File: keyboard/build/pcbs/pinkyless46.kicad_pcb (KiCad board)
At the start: 2 copper layers, 108.1 x 162.6 mm, 49 parts

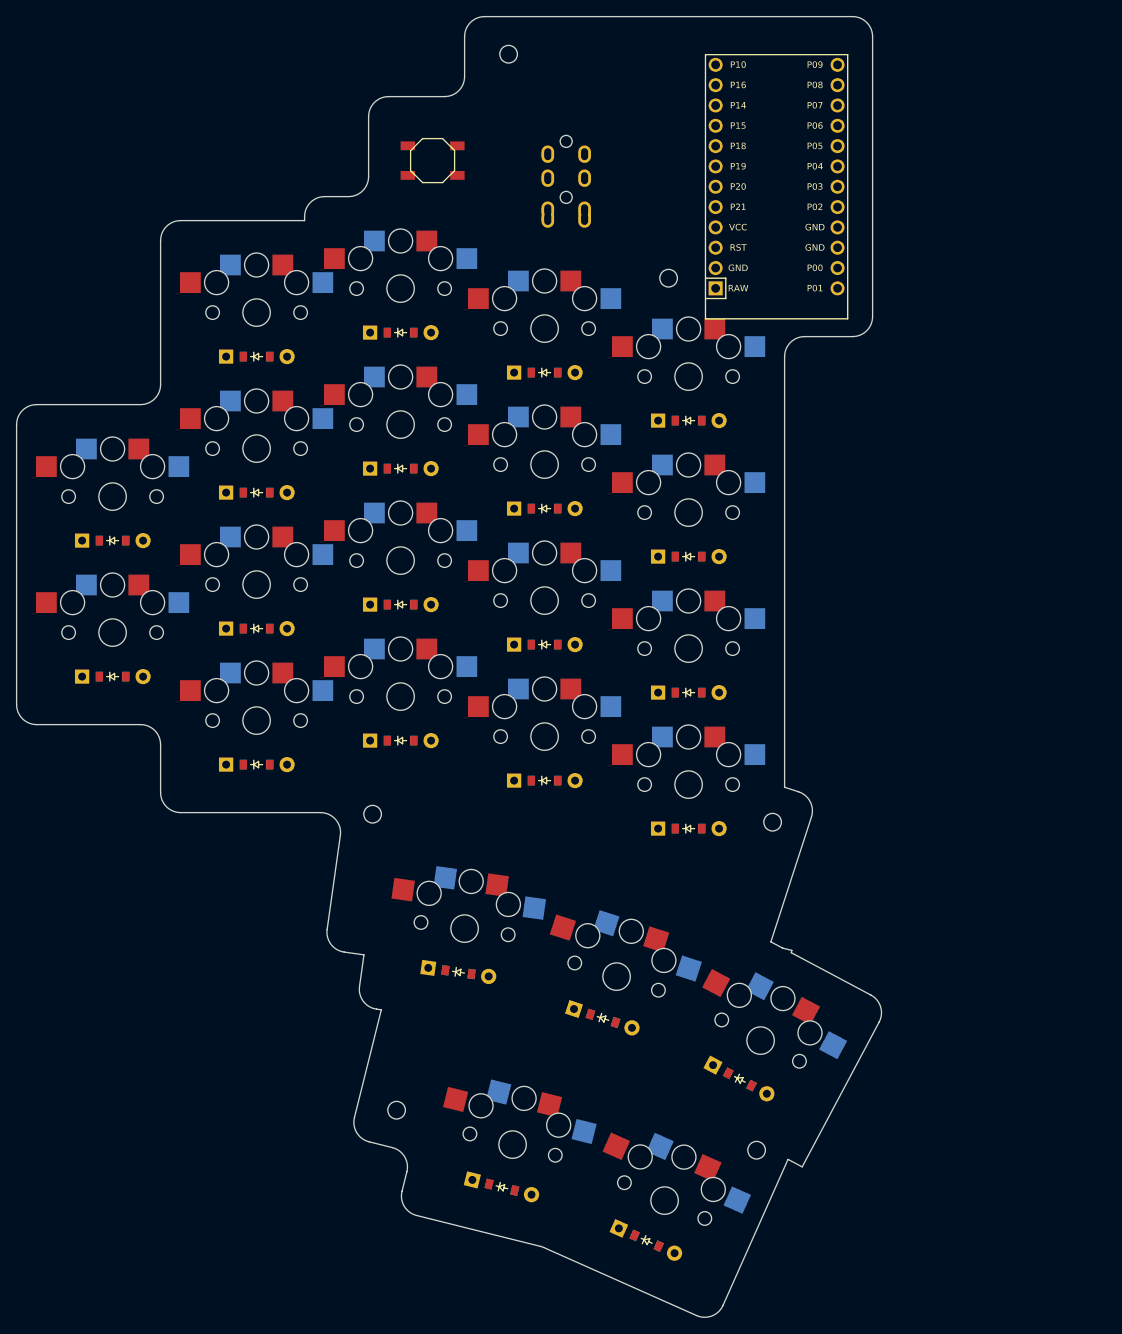
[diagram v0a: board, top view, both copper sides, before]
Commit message: Move thumb cluster outward to align with the middle column
The cluster sat too far inboard: the innermost thumb key was at x=104,
between the index and inner columns, so the thumb had to reach across
the board rather than drop straight down.

Re-anchor the thumb zone from matrix_index_bottom to matrix_middle_bottom
and give t1 an x-shift of exactly 0. That puts t1 directly below the
middle column - the column with the largest stagger, i.e. the one sitting
furthest forward - and makes the alignment a structural property of the
config rather than a constant to maintain by hand. Re-stagger the matrix
later and the cluster tracks it automatically.

The cluster translates rigidly 8 mm outward, so the arc geometry and thumb
reach distances are unchanged (furthest key still 42.2 mm from thumb home).
Screw positions were re-derived with find_mounts.py, since one hole ended
up on a pad after the move; the thinnest plate web actually improved from
2.45 mm to 3.26 mm. Board is now 107.0 x 162.6 mm per half.

Case STLs, QMK keyboard.json and previews regenerated. All five checks pass.

Co-Authored-By: Claude Opus 5 <noreply@anthropic.com>
Claude-Session: https://claude.ai/code/session_01TKXtddA7pBLooPYbDwxvxo
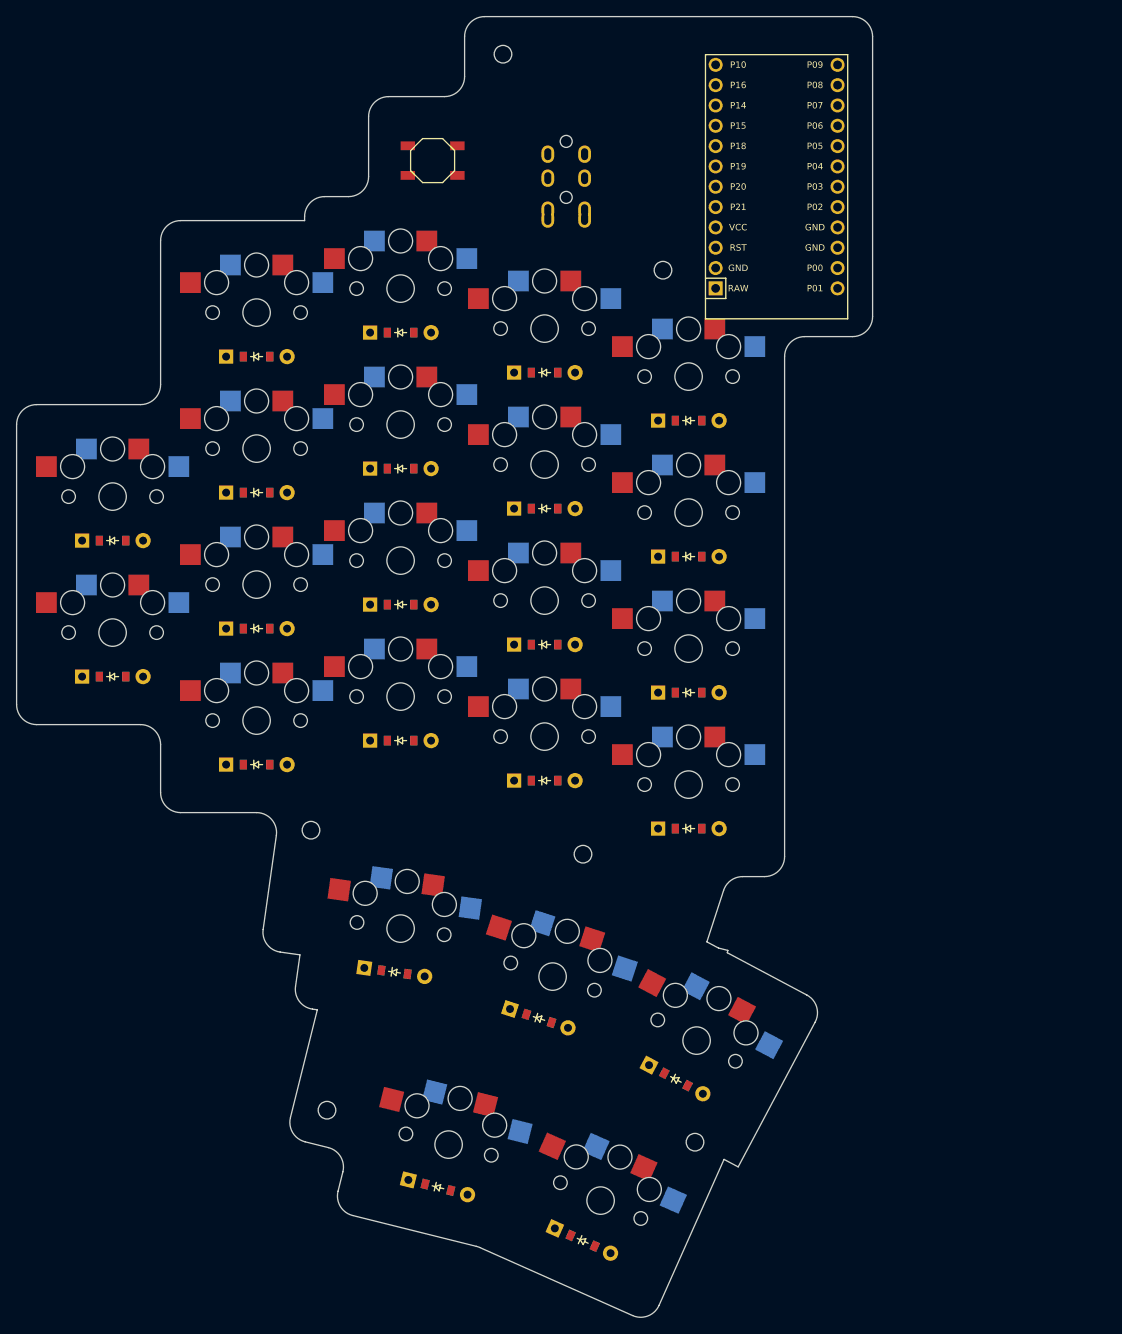
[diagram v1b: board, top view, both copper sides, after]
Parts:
- moved D19 8.00 mm to (95.2, 185.4)
- moved D20 8.00 mm to (113.3, 191.2)
- moved D21 8.00 mm to (130.4, 198.9)
- moved D22 8.00 mm to (100.7, 212.3)
- moved D23 8.00 mm to (118.8, 219.0)
- moved S19 8.00 mm to (96.0, 180.0)
- moved S20 8.00 mm to (115.0, 186.0)
- moved S21 8.00 mm to (133.0, 194.0)
- moved S22 8.00 mm to (102.0, 207.0)
- moved S23 8.00 mm to (121.0, 214.0)
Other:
- board size 108.1 x 162.6 mm -> 107 x 162.6 mm

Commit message: Move thumb cluster inboard to start where the finger matrix ends
Previous attempt moved the cluster the wrong way. The requirement is that
the NEAREST thumb key line up with the LAST (most inboard) finger column,
with the cluster extending inboard from there - not tucked back underneath
the finger columns. Before this, the cluster spanned x=96..133, so its far
end coincided with the inner column and its near end sat under the middle
column.

Re-anchor the thumb zone to matrix_inner_bottom with t1 at an x-shift of
exactly 0. t1 now sits at x=132, the same x as the inner column, and the
cluster runs inboard to x=169. As with the previous anchoring, this is
structural: add or remove a finger column and the cluster still begins
where the matrix ends.

The cluster translates rigidly, so the arc shape and thumb reach are
unchanged (furthest key still 42.2 mm from thumb home) and there are no
keycap or switch-body collisions. The board grows to 136.1 x 162.6 mm per
half; the extra width is the ~37 mm the cluster now reaches inboard. Halves
still clear each other by 38.8 mm.

Screw positions re-derived. Case STLs, QMK keyboard.json and previews
regenerated. All five checks pass.

Co-Authored-By: Claude Opus 5 <noreply@anthropic.com>
Claude-Session: https://claude.ai/code/session_01TKXtddA7pBLooPYbDwxvxo
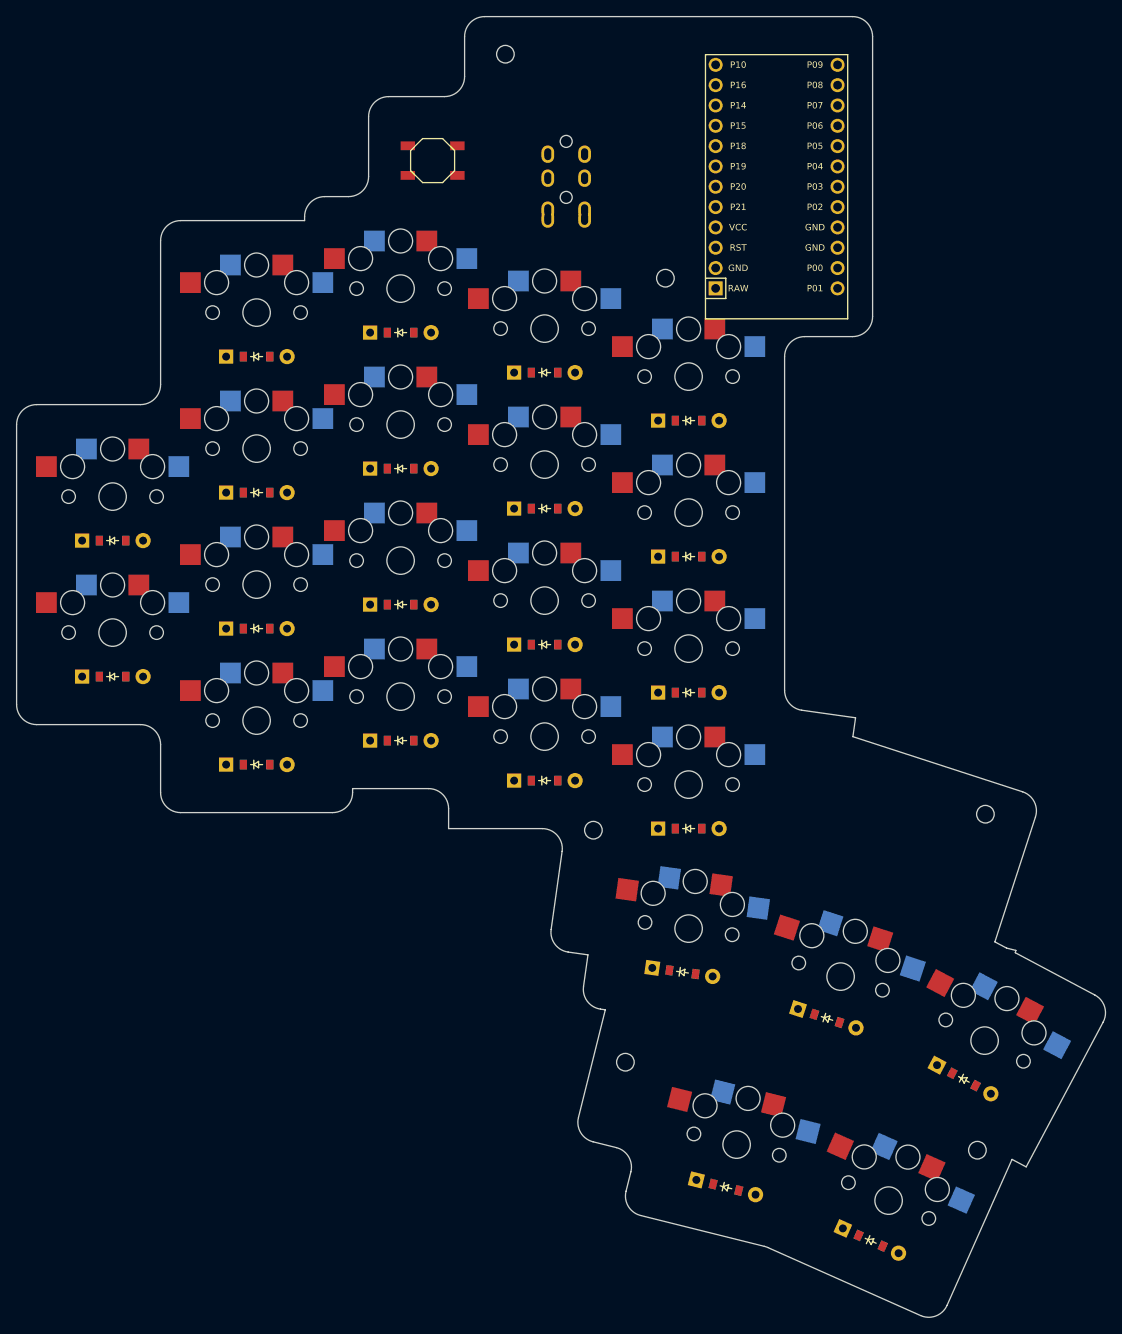
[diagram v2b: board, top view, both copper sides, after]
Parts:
- moved D20 36.0 mm to (149.3, 191.2)
- moved D19 36.0 mm to (131.2, 185.4)
- moved D21 36.0 mm to (166.4, 198.9)
- moved D22 36.0 mm to (136.7, 212.3)
- moved D23 36.0 mm to (154.8, 219.0)
- moved S19 36.0 mm to (132.0, 180.0)
- moved S20 36.0 mm to (151.0, 186.0)
- moved S21 36.0 mm to (169.0, 194.0)
- moved S22 36.0 mm to (138.0, 207.0)
- moved S23 36.0 mm to (157.0, 214.0)
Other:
- board size 107 x 162.6 mm -> 136.1 x 162.6 mm
